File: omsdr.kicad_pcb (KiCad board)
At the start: 2 copper layers, 50 x 50 mm, 58 parts, among them J1 I/Q Out, J2 ANT, J3 ISP, J4 LO, J5 I/Q Out, J8 IO, SW1 SW_SPST, SW2 SW_SPST, T1 CX2074NL, U1 LT6231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

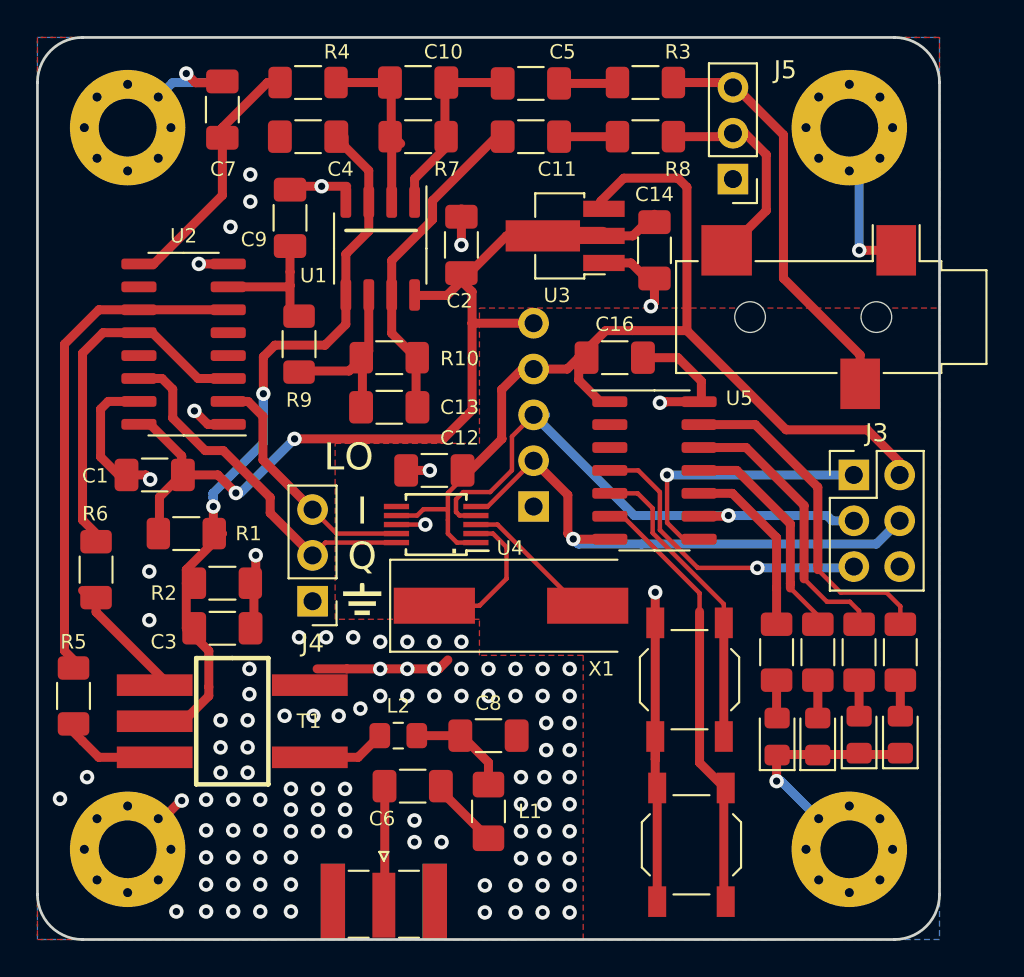
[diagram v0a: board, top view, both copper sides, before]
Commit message: Cleanup to satisfy DRC
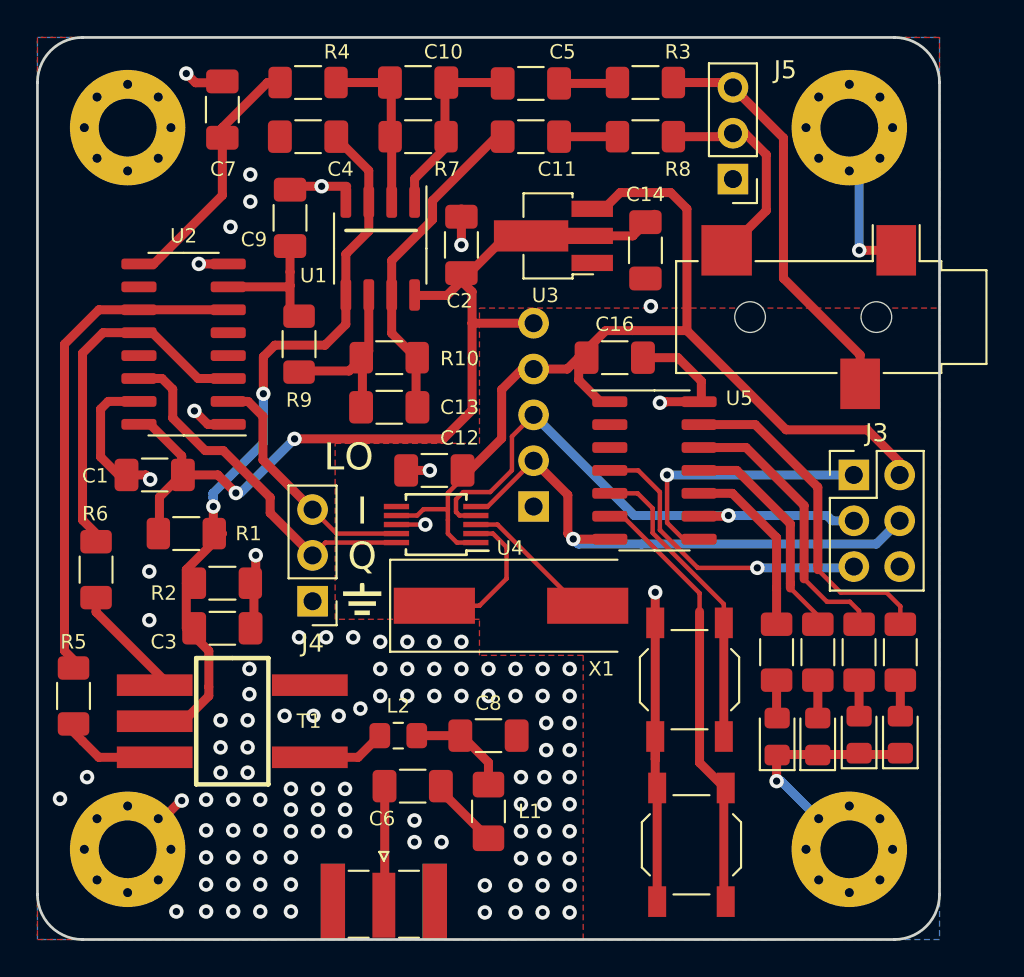
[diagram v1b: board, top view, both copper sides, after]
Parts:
- moved U3 0.65 mm to (128.6, 61.0)
- moved C14 0.50 mm to (133.7, 61.8)
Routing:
- net GND: track 97.9 -> 77.8 mm
- net +5V: track 58.4 -> 49.5 mm
- net /Vhalf: track 43.4 -> 40.6 mm
- net +3V3: track 58.0 -> 57.2 mm
- net Net-(R6-Pad2): track 8.00 -> 7.29 mm
- net /SCK: track 31.6 -> 30.9 mm
- net Net-(J5-Pad3): track 23.4 -> 22.8 mm
- net /MISO: track 15.7 -> 15.2 mm
- net Net-(C10-Pad1): track 9.24 -> 8.70 mm
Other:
- board text removed: "."

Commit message: Setting solder mask clearance to 0
Board house will use their own value and modify the gerbers.
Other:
- rule pad_to_mask_clearance: 0.2 -> 0
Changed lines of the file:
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@@
       (dielectric_constraints no)
     )
-    (pad_to_mask_clearance 0.2)
-    (solder_mask_min_width 0.25)
+    (pad_to_mask_clearance 0)
     (pcbplotparams
       (layerselection 0x00012f0_ffffffff)

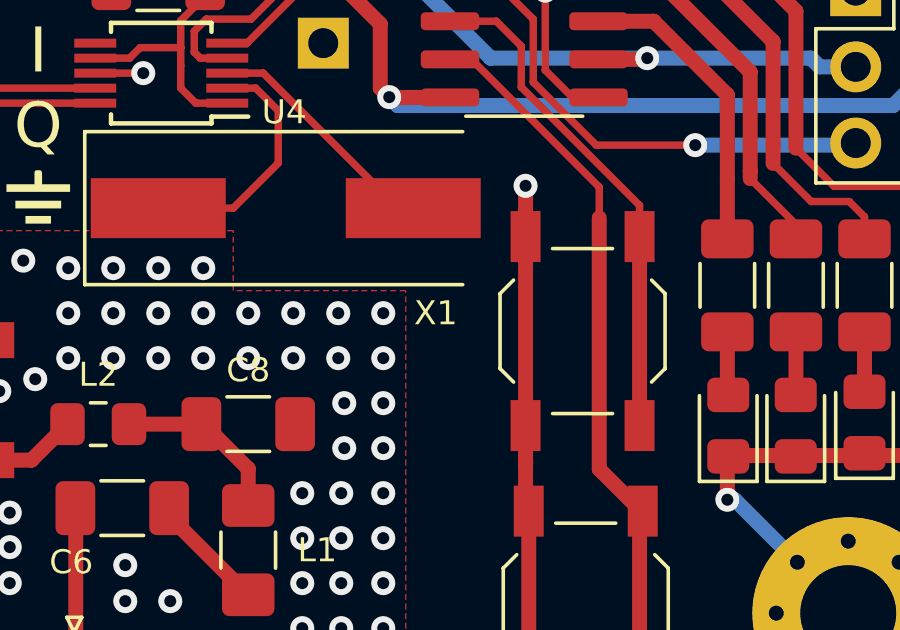
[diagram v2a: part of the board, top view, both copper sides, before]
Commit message: Using crystal footprint from the KiCad library (pcb & 3d model)
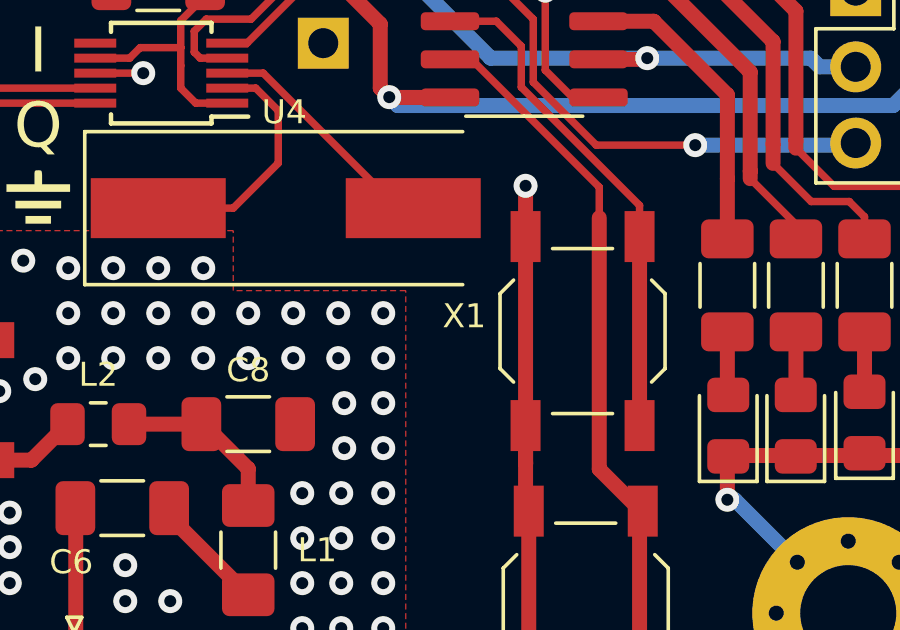
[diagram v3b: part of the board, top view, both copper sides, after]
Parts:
- X1: footprint Crystals:Crystal_SMD_HC49-SD -> Crystal:Crystal_SMD_HC49-SD
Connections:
- net /SDA renamed /MOSI

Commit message: Replacing push buttons with current kicad footprints and 3d models
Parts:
- SW1: value SW_SPST -> LEFT; footprint Buttons_Switches_SMD:SW_SPST_TL3342 -> Button_Switch_SMD:SW_SPST_TL3342
- SW2: value SW_SPST -> RIGHT; footprint Buttons_Switches_SMD:SW_SPST_TL3342 -> Button_Switch_SMD:SW_SPST_TL3342
